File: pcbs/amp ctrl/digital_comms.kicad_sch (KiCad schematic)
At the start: 54 parts, among them J15 RJ45_Shielded, J17 RJ45_Shielded, J88 RJ45_Shielded, Q33 MMBT3904, Q34 MMBT3904, Q35 MMBT3906, Q38 MMBT3904, U21 74LVC2G17, U47 74LVC2G17, U62 FIN1028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

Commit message: Misc. cleanup for mfg & improvements
Minor backplane pinout doc corrections (SCKO5 polarity, clarified some descriptions)
Backplane: Added differential- and common-mode (to standoffs) power filtering, for EMI escaping over power wiring
Amp ctrl: Changed DAC testpoints from individual pads to Keystone 5019 for easier probing
Corrected part numbers, DNP vs. non-BOM-item indications, other misc. BOM issues
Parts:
- TP165, TP63: now left out of the parts list
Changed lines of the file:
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@@
 		(unit 1)
 		(exclude_from_sim no)
-		(in_bom yes)
+		(in_bom no)
 		(on_board yes)
 		(dnp no)
@@
 		(unit 1)
 		(exclude_from_sim no)
-		(in_bom yes)
+		(in_bom no)
 		(on_board yes)
 		(dnp no)

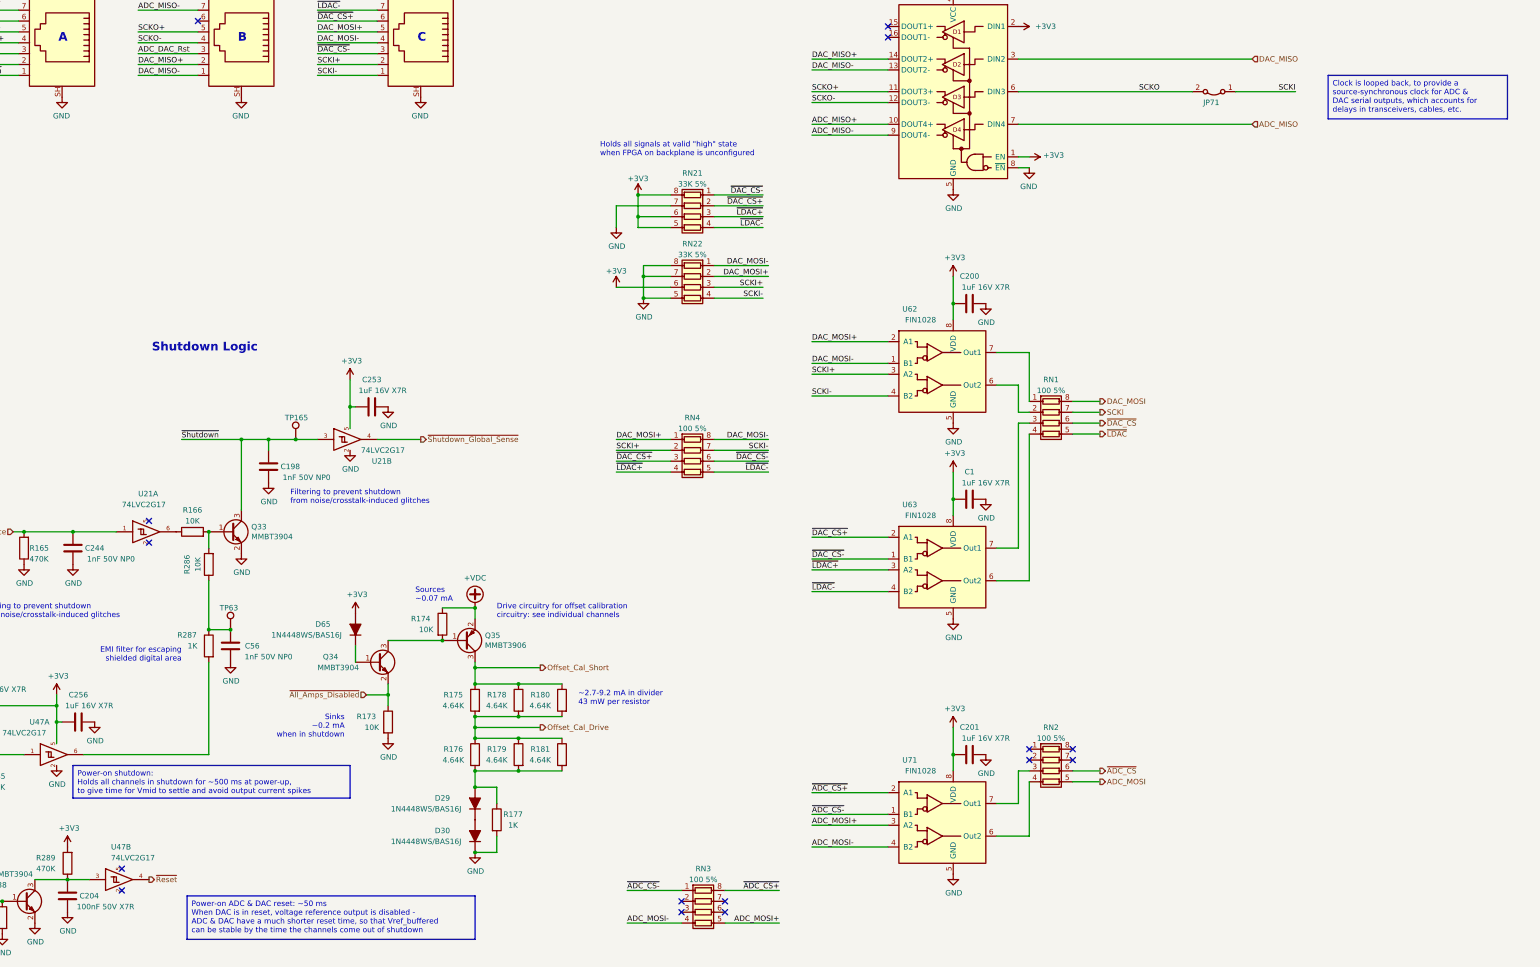
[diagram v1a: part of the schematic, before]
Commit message: Updated KiCAD file versions to 9.0
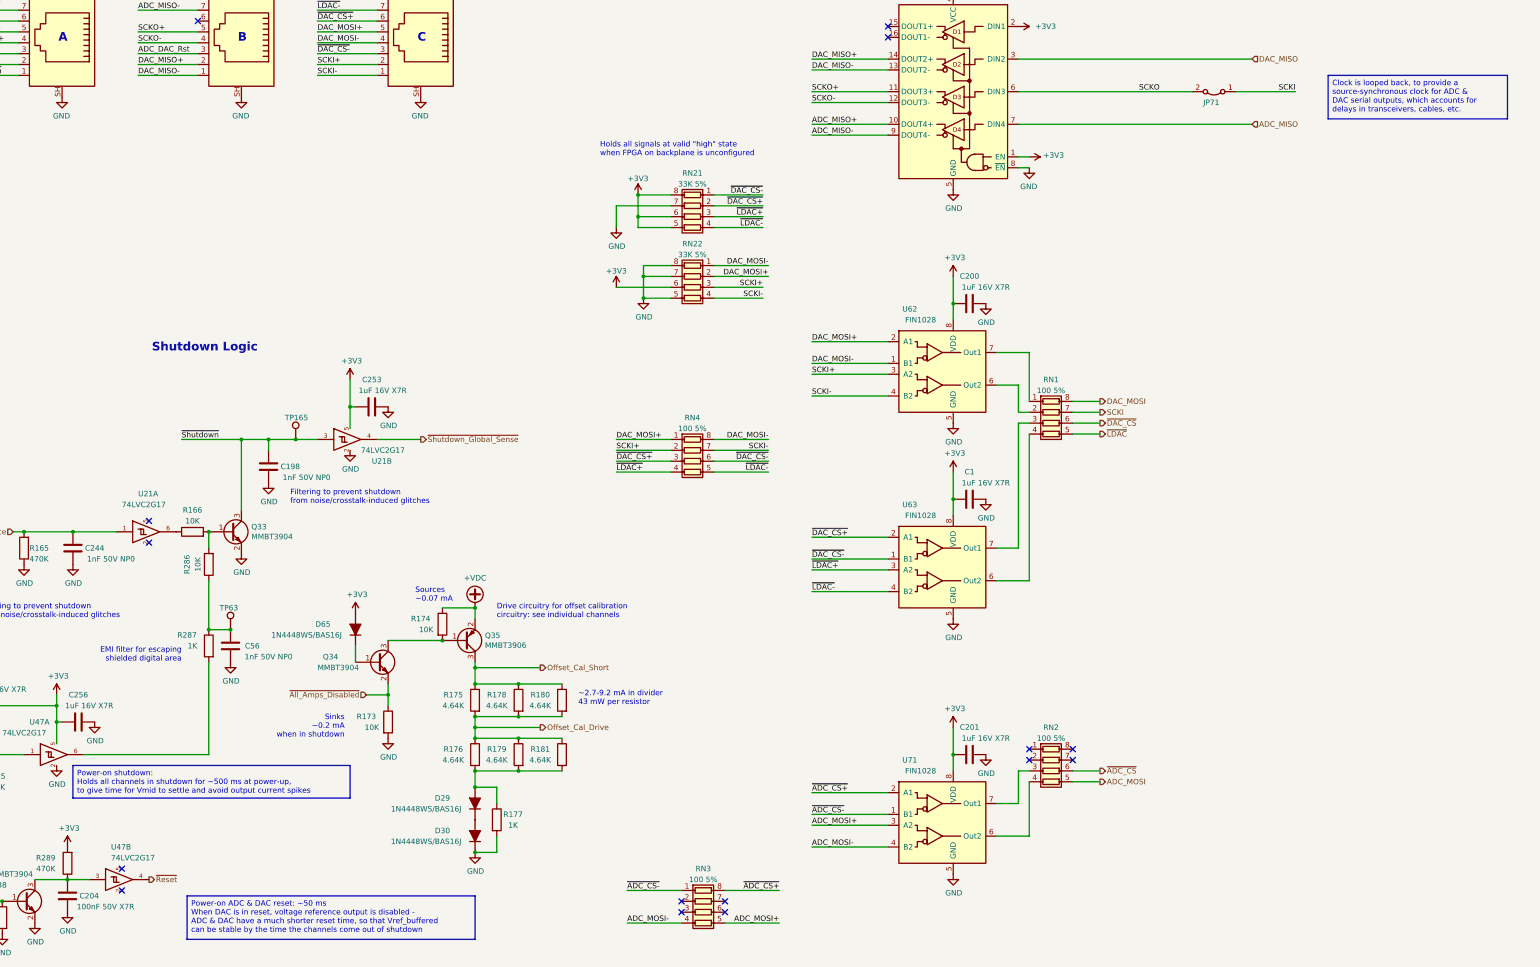
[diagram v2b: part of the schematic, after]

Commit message: Moved all project-specific symbols & footprints into new "shim" libraries Updated projects to reference the new "shim" library
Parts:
- D29, D30, D65: footprint Don_std:D_SOD-323F -> shim:D_SOD-323F
- J15, J17, J88: footprint Martinos:RJ45_TE_x-406541-x_Horizontal -> shim:RJ45_TE_x-406541-x_Horizontal
- Q33, Q34, Q35: footprint Martinos_std:SOT-23 -> Package_TO_SOT_SMD:SOT-23
- Q38: footprint Don_std:SOT-23 -> Package_TO_SOT_SMD:SOT-23
- RN1, RN2, RN3, RN4: footprint Martinos_std:R_Array_Concave_4x0603 -> Resistor_SMD:R_Array_Concave_4x0603
- RN21, RN22: footprint Don_std:R_Array_Concave_4x0603 -> Resistor_SMD:R_Array_Concave_4x0603
- U21, U47: footprint Martinos_std:SOT-23-6 -> Package_TO_SOT_SMD:SOT-23-6
- U62, U63, U71: footprint Don_std:SOIC-8_3.9x4.9mm_P1.27mm -> Package_SO:SOIC-8_3.9x4.9mm_P1.27mm
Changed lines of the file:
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@@
 			)
 		)
-		(property "Footprint" "Martinos_std:R_Array_Concave_4x0603"
+		(property "Footprint" "Resistor_SMD:R_Array_Concave_4x0603"
 			(at 284.48 154.305 90)
 			(effects
@@
 			)
 		)
-		(property "Footprint" "Don_std:SOIC-8_3.9x4.9mm_P1.27mm"
+		(property "Footprint" "Package_SO:SOIC-8_3.9x4.9mm_P1.27mm"
 			(at 284.48 153.67 0)
 			(effects
@@
 			)
 		)
-		(property "Footprint" "Martinos_std:R_Array_Concave_4x0603"
+		(property "Footprint" "Resistor_SMD:R_Array_Concave_4x0603"
 			(at 284.48 235.585 90)
 			(effects
@@
 			)
 		)
-		(property "Footprint" "Don_std:SOIC-8_3.9x4.9mm_P1.27mm"
+		(property "Footprint" "Package_SO:SOIC-8_3.9x4.9mm_P1.27mm"
 			(at 284.48 199.39 0)
 			(effects
@@
 			)
 		)
-		(property "Footprint" "Don_std:SOIC-8_3.9x4.9mm_P1.27mm"
+		(property "Footprint" "Package_SO:SOIC-8_3.9x4.9mm_P1.27mm"
 			(at 284.48 259.08 0)
 			(effects
@@
 			)
 		)
-		(property "Footprint" "Martinos_std:R_Array_Concave_4x0603"
+		(property "Footprint" "Resistor_SMD:R_Array_Concave_4x0603"
 			(at 200.66 163.195 90)
 			(effects
@@
 			)
 		)
-		(property "Footprint" "Martinos_std:R_Array_Concave_4x0603"
+		(property "Footprint" "Resistor_SMD:R_Array_Concave_4x0603"
 			(at 203.2 268.605 90)
 			(effects
@@
 			)
 		)
-		(property "Footprint" "Martinos:RJ45_TE_x-406541-x_Horizontal"
+		(property "Footprint" "shim:RJ45_TE_x-406541-x_Horizontal"
 			(at 95.25 52.705 90)
 			(effects
@@
 			)
 		)
-		(property "Footprint" "Martinos:RJ45_TE_x-406541-x_Horizontal"
+		(property "Footprint" "shim:RJ45_TE_x-406541-x_Horizontal"
 			(at 137.16 52.705 90)
 			(effects
@@
 			)
 		)
-		(property "Footprint" "Martinos:RJ45_TE_x-406541-x_Horizontal"
+		(property "Footprint" "shim:RJ45_TE_x-406541-x_Horizontal"
 			(at 53.34 52.705 90)
 			(effects
@@
 			)
 		)
-		(property "Footprint" "Martinos_std:SOT-23-6"
+		(property "Footprint" "Package_TO_SOT_SMD:SOT-23-6"
 			(at 52.07 219.71 0)
 			(effects
@@
 			)
 		)
-		(property "Footprint" "Martinos_std:SOT-23-6"
+		(property "Footprint" "Package_TO_SOT_SMD:SOT-23-6"
 			(at 67.31 248.92 0)
 			(effects
@@
 			)
 		)
-		(property "Footprint" "Martinos_std:SOT-23-6"
+		(property "Footprint" "Package_TO_SOT_SMD:SOT-23-6"
 			(at 120.65 146.05 0)
 			(effects
@@
 			)
 		)
-		(property "Footprint" "Martinos_std:SOT-23-6"
+		(property "Footprint" "Package_TO_SOT_SMD:SOT-23-6"
 			(at 73.66 167.64 0)
 			(effects
@@
 			)
 		)
-		(property "Footprint" "Martinos_std:SOT-23"
+		(property "Footprint" "Package_TO_SOT_SMD:SOT-23"
 			(at 97.79 169.545 0)
 			(effects
@@
 			)
 		)
-		(property "Footprint" "Martinos_std:SOT-23"
+		(property "Footprint" "Package_TO_SOT_SMD:SOT-23"
 			(at 152.4 191.135 0)
 			(effects
@@
 			)
 		)
-		(property "Footprint" "Martinos_std:SOT-23"
+		(property "Footprint" "Package_TO_SOT_SMD:SOT-23"
 			(at 132.08 200.025 0)
 			(effects
@@
 			)
 		)
-		(property "Footprint" "Don_std:D_SOD-323F"
+		(property "Footprint" "shim:D_SOD-323F"
 			(at 149.86 231.14 0)
 			(effects
@@
 			)
 		)
-		(property "Footprint" "Don_std:D_SOD-323F"
+		(property "Footprint" "shim:D_SOD-323F"
 			(at 149.86 238.76 0)
 			(effects
@@
 			)
 		)
-		(property "Footprint" "Don_std:D_SOD-323F"
+		(property "Footprint" "shim:D_SOD-323F"
 			(at 121.92 190.5 0)
 			(effects
@@
 			)
 		)
-		(property "Footprint" "Don_std:SOT-23"
+		(property "Footprint" "Package_TO_SOT_SMD:SOT-23"
 			(at 49.53 255.905 0)
 			(effects
@@
 			)
 		)
-		(property "Footprint" "Don_std:R_Array_Concave_4x0603"
+		(property "Footprint" "Resistor_SMD:R_Array_Concave_4x0603"
 			(at 200.66 122.555 90)
 			(effects
@@
 			)
 		)
-		(property "Footprint" "Don_std:R_Array_Concave_4x0603"
+		(property "Footprint" "Resistor_SMD:R_Array_Concave_4x0603"
 			(at 200.66 106.045 90)
 			(effects

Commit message: Finished migrating footprint names
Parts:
- U64: footprint Martinos_std:TSSOP-16_4.4x5mm_P0.65mm -> Package_SO:TSSOP-16_4.4x5mm_P0.65mm
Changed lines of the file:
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@@
 			)
 		)
-		(property "Footprint" "Martinos_std:TSSOP-16_4.4x5mm_P0.65mm"
+		(property "Footprint" "Package_SO:TSSOP-16_4.4x5mm_P0.65mm"
 			(at 264.16 88.9 0)
 			(effects
